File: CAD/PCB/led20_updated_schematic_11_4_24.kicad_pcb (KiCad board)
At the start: 2 copper layers, 55 x 55 mm, 33 parts, among them U6 B2B-PH-K-S, U7 B2B-PH-K-S

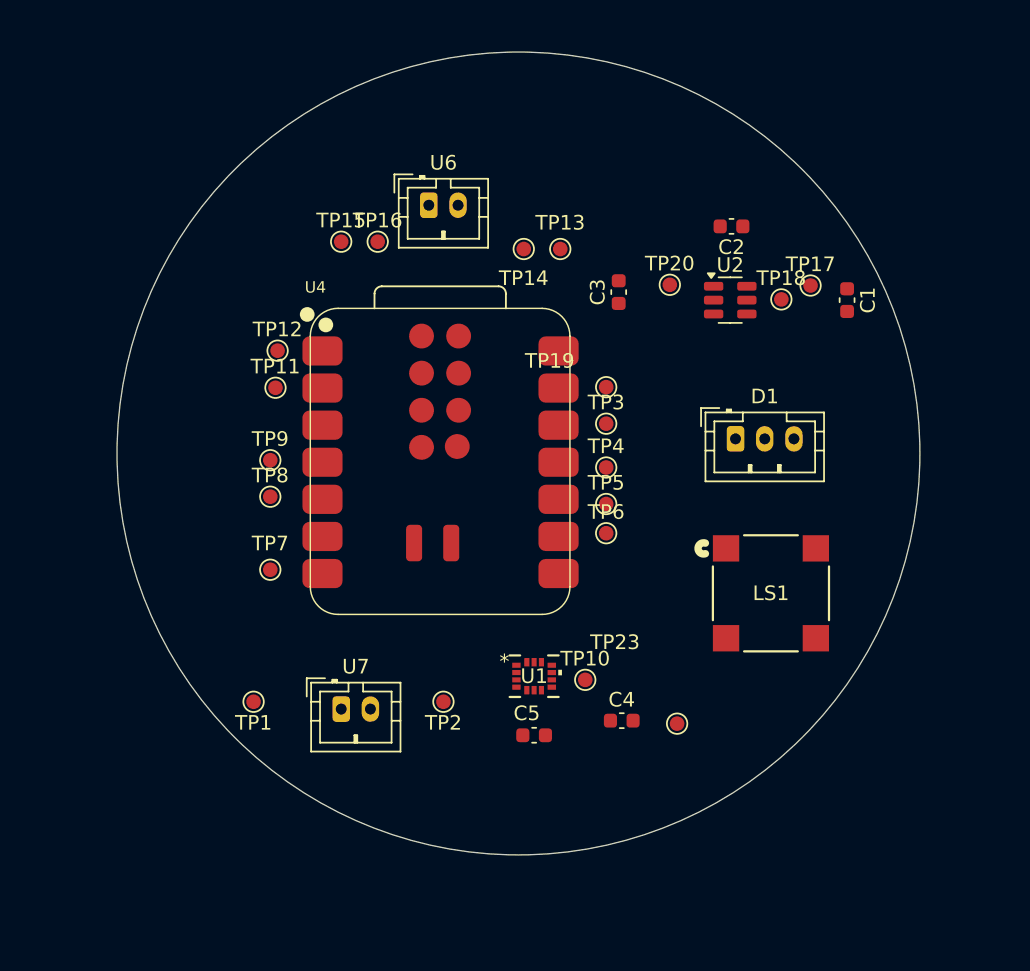
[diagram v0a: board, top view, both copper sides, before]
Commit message: PCB and Schematic Update
Updated PCB with traces and ground planes. Needs review. Battery symbol for schematic was removed - JST connector remains in its place.
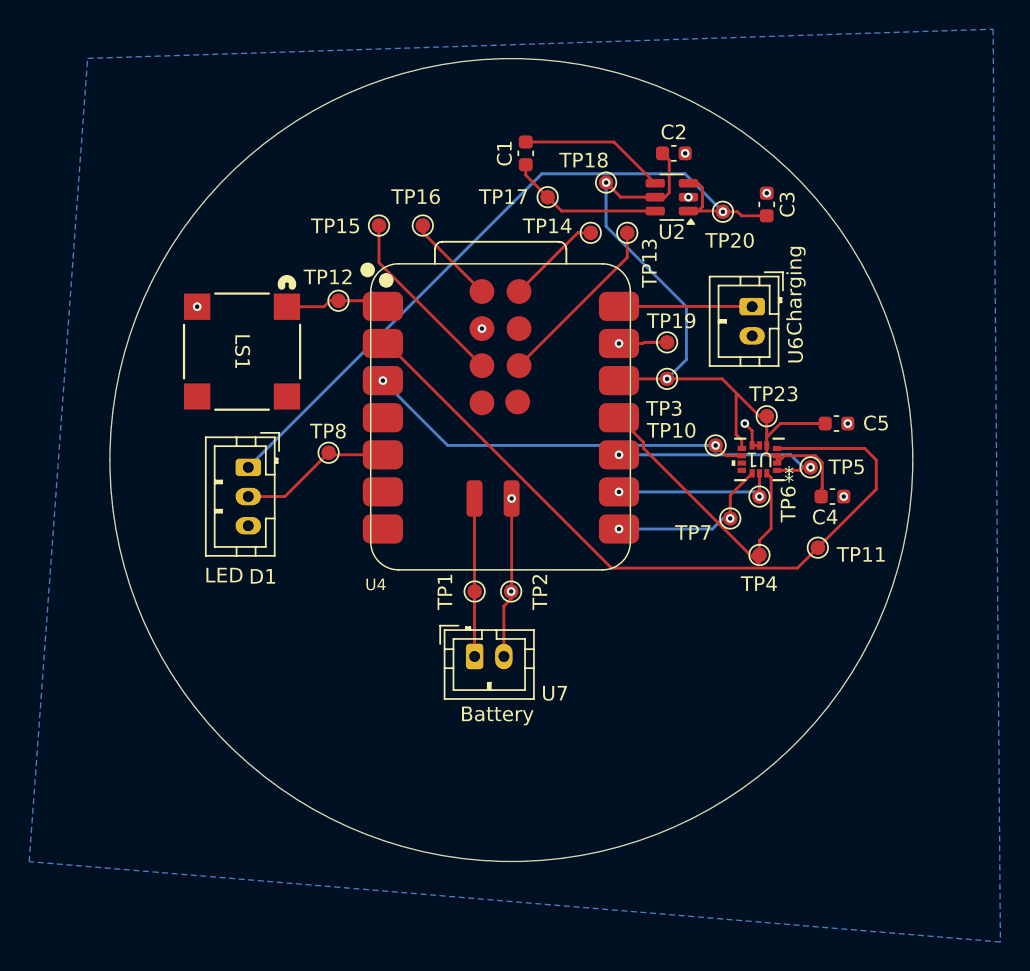
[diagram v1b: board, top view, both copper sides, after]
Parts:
- removed TP9: ~, TestPoint:TestPoint_Pad_D1.0mm
- moved LS1 39.8 mm to (124.2, 71.0), turned to -90 degrees
- moved TP11 38.7 mm to (163.6, 84.5)
- moved D1 33.4 mm to (124.6, 79.0), turned to -90 degrees
- moved TP7 31.7 mm to (157.6, 82.5)
- moved C5 29.7 mm to (164.9, 76.0), turned to 180 degrees
- moved C1 24.2 mm to (143.6, 57.5), turned to 90 degrees
- moved U6 23.2 mm to (159.1, 68.0), turned to -90 degrees
- moved TP23 21.9 mm to (160.1, 75.5), turned to 180 degrees
- moved U1 21.4 mm to (159.6, 78.4), turned to 180 degrees
- moved C4 21.1 mm to (164.6, 81.0), turned to 180 degrees
- moved TP17 19.0 mm to (145.1, 60.5), turned to 180 degrees
- moved TP10 18.4 mm to (156.6, 77.5), turned to 180 degrees
- moved TP1 16.9 mm to (140.1, 87.5)
- moved TP18 14.4 mm to (149.1, 59.5), turned to 180 degrees
- moved TP5 14.2 mm to (163.1, 79.0)
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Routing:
- net 3.3V: track 0.00 -> 52.8 mm, vias 0 -> 2
- net Net-(U1-INT1): track 0.00 -> 51.5 mm
- net +5V: track 0.00 -> 50.9 mm, vias 0 -> 1
- net Net-(U1-INT2): track 0.00 -> 26.7 mm, vias 0 -> 2
- net Net-(U1-SDA): track 0.00 -> 20.5 mm
- net GND: track 0.00 -> 16.7 mm, vias 0 -> 11
- net Net-(U1-SDO/SA0): track 0.00 -> 15.8 mm, vias 0 -> 2
- net unconnected-(TP15-Pad1): track 0.00 -> 12.5 mm
- net unconnected-(TP13-Pad1): track 0.00 -> 12.2 mm
- net Net-(U1-CS): track 0.00 -> 11.7 mm, vias 0 -> 2
- net Net-(U1-SCL): track 0.00 -> 11.6 mm, vias 0 -> 2
- net VBATT: track 0.00 -> 10.8 mm
- net Net-(U2-C+): track 0.00 -> 10.6 mm
- net 3.3V Data (D4): track 0.00 -> 10.5 mm
- net Net-(U2-C-): track 0.00 -> 10.0 mm
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- added copper zone on B.Cu, net GND
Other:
- board text added: "Battery"
- board text added: "Charging"
- board text added: "LED"

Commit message: Update to PCB
Moved caps closer to ICs
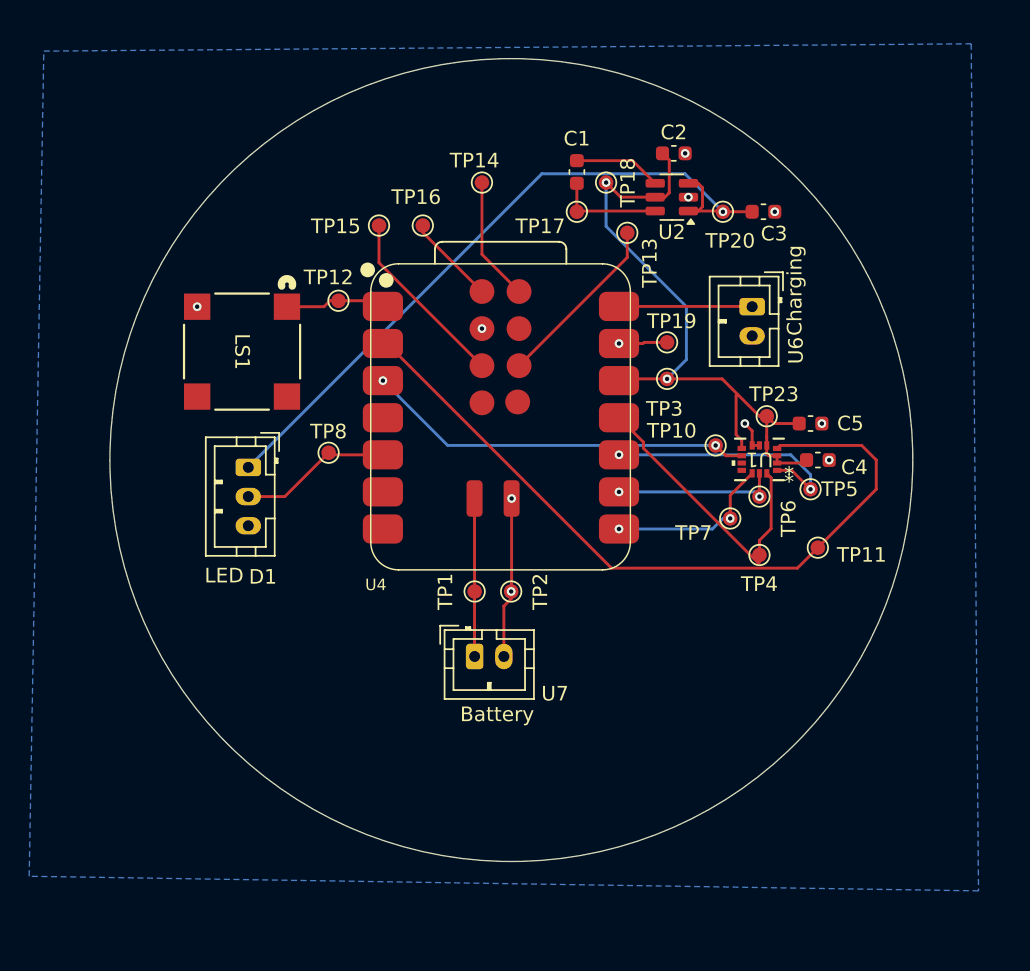
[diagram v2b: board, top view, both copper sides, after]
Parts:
- moved TP14 8.21 mm to (140.6, 59.5)
- moved C1 3.72 mm to (147.1, 58.7)
- moved C4 2.69 mm to (163.6, 78.5)
- moved TP17 2.24 mm to (147.1, 61.5)
- moved C5 1.78 mm to (163.1, 76.0)
- moved TP5 1.50 mm to (163.1, 80.5)
- moved C3 0.55 mm to (159.9, 61.5), turned to 180 degrees
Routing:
- net 3.3V: track 52.8 -> 47.6 mm
- net Net-(U2-C-): track 10.0 -> 6.00 mm
- net Net-(U2-C+): track 10.6 -> 7.26 mm
- net unconnected-(TP14-Pad1): track 6.57 -> 8.51 mm
- net Net-(U1-SDO/SA0): track 15.8 -> 17.5 mm
- net +5V: track 50.9 -> 49.8 mm

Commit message: PCB
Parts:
- C4, C5, TP10, TP11, TP4, TP5, TP6, TP7, U1: moved to B.Cu
- TP21: renamed from TP23; moved to B.Cu
- moved D1 34.6 mm to (158.8, 73.2)
- moved TP20 33.7 mm to (160.5, 95.0)
- moved TP17 33.7 mm to (153.3, 94.5)
- moved C1 33.6 mm to (153.3, 91.8)
- moved C2 31.8 mm to (156.8, 89.1)
- moved U2 31.7 mm to (156.8, 92.0)
- moved C3 30.8 mm to (160.6, 92.2), turned to -90 degrees
- moved TP18 30.0 mm to (153.6, 89.1)
- moved LS1 25.9 mm to (138.0, 93.0), turned to 0 degrees
- moved C5 23.9 mm to (143.7, 89.7), turned to -90 degrees
- moved C4 23.5 mm to (145.5, 93.4), turned to 90 degrees
- moved TP11 21.5 mm to (143.7, 92.3), turned to -90 degrees
- moved TP5 20.4 mm to (147.4, 93.4), turned to -90 degrees
- moved TP12 20.0 mm to (133.6, 87.3)
- moved TP21 19.6 mm to (144.5, 87.2), turned to 90 degrees
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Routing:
- net 3.3V Data (D4): track 10.5 -> 42.1 mm, vias 0 -> 2
- net Net-(U1-INT1): track 51.7 -> 28.2 mm, vias 0 -> 1
- net Net-(U4-LP_GPIO0/GPIO0/A0/D0): track 6.90 -> 28.2 mm
- net GND: track 16.7 -> 37.9 mm, vias 11 -> 12
- net +5V: track 49.8 -> 29.5 mm, vias 1 -> 0
- net VBATT: track 10.8 -> 23.3 mm
- net Net-(U1-CS): track 11.7 -> 7.56 mm, vias 2 -> 1
- net Net-(U2-C-): track 6.00 -> 2.58 mm
- net Net-(U1-SDO/SA0): track 17.5 -> 20.8 mm, vias 2 -> 1
- net Net-(U2-C+): track 7.26 -> 4.47 mm
- net Net-(U1-INT2): track 26.7 -> 28.4 mm, vias 2 -> 1
- net unconnected-(TP15-Pad1): track 12.5 -> 10.9 mm, vias 0 -> 1
- net unconnected-(TP16-Pad1): track 6.20 -> 5.29 mm, vias 0 -> 1
- net unconnected-(TP14-Pad1): track 8.51 -> 9.17 mm
- net 3.3V: track 47.6 -> 48.3 mm, vias 2 -> 3
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- added copper zone on F.Cu, net GND
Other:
- board size 55 x 55 mm -> 30 x 35 mm
